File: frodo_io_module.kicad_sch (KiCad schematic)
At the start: 83 parts, among them J1 Molex MicroFit 2x3, J1 SWD, J2 Molex MicroFit 2x3, J4 JST-GH 4Pin, SW1 SW_DIP_x06, U1 AZ1117H-ADJ, U1 STM32F072RBT6, U3 AZ1117-3.3, U4 W25Q128JVP, U5 MCP2562-E-SN, U6 L7805, U7 L7805, Y1 8MHz 12pF

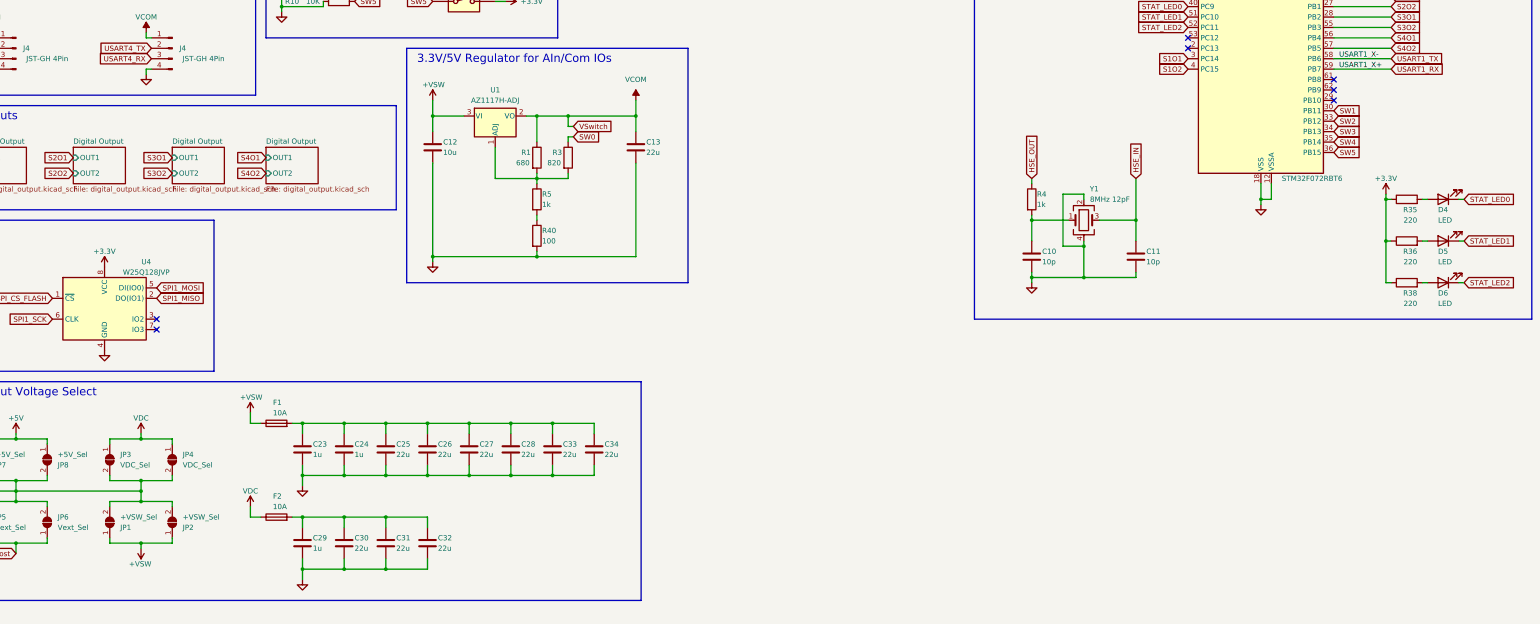
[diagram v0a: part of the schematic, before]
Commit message: Add boost converter schematics
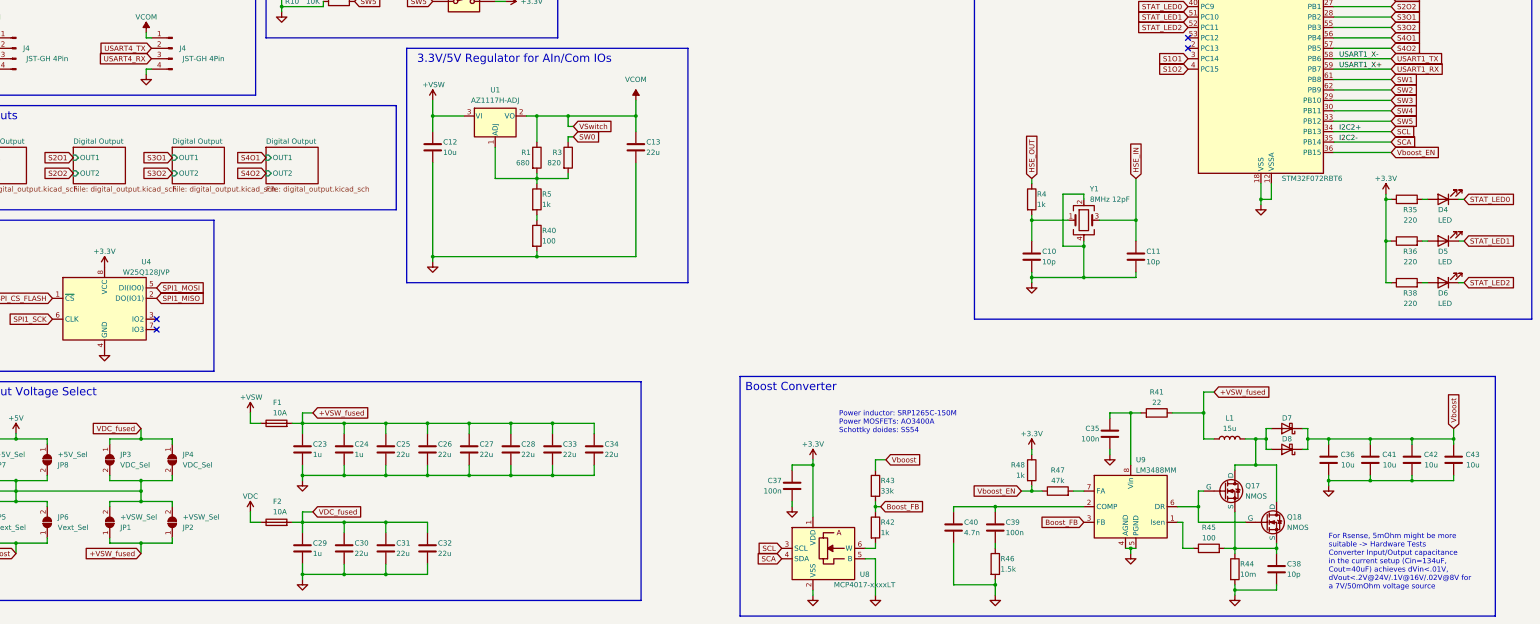
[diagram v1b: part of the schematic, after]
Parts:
- added C35, C37, C39: 100n, symbol Device:C
- added C36, C41, C42, C43: 10u, symbol Device:C
- added C38: 10p, symbol Device:C
- added C40: 4.7n, symbol Device:C
- added D7, D8: D_Schottky, symbol Device:D_Schottky
- added L1: 15u, symbol Device:L
- added Q17, Q18: NMOS, symbol Simulation_SPICE:NMOS
- added R41: 22, symbol Device:R
- added R42, R48: 1k, symbol Device:R
- added R43: 33k, symbol Device:R
- added R44: 10m, symbol Device:R
- added R45: 100, symbol Device:R
- added R46: 1.5k, symbol Device:R
- added R47: 47k, symbol Device:R
- added U8: MCP4017-xxxxLT, Package_TO_SOT_SMD:SOT-363_SC-70-6, symbol Potentiometer_Digital:MCP4017-xxxxLT
- added U9: LM3488MM, symbol frodo_io_module:LM3488MM
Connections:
- net +3.3V: now also C37.1, R48.1, U8.1 (VDD)
- net +VSW: no longer JP1.1 (A), JP2.1 (A)
- net GND: now also C35.2, C36.2, C37.2, C38.2, C40.2, C41.2, C42.2, C43.2, R44.2, R46.2, U8.2 (VSS), U8.5 (B), U9.4 (AGND), U9.5 (PGND)
- net SW1: now also U1.61 (PB8); no longer U1.30 (PB11)
- net SW2: now also U1.62 (PB9); no longer U1.33 (PB12)
- net SW3: now also U1.29 (PB10); no longer U1.34 (PB13)
- net SW4: now also U1.30 (PB11); no longer U1.35 (PB14)
- net SW5: now also U1.33 (PB12); no longer U1.36 (PB15)
- net VDC: no longer JP3.1 (A), JP4.1 (A)
- net Vboost: now also C36.1, C41.1, C42.1, C43.1, D7.1 (K), D8.1 (K), R43.1
- net +VSW_fused: now reaches C23.1, C24.1, C25.1, C26.1, C27.1, C28.1, C33.1, C34.1, F1.2
- net +VSW_fused: now also JP1.1 (A), JP2.1 (A), L1.1, R41.1
- net VDC_fused: now reaches C29.1, C30.1, C31.1, C32.1, F2.2
- net VDC_fused: now also JP3.1 (A), JP4.1 (A)
- new net: C35.1, R41.2, U9.8 (Vin)
- new net: R45.1, U9.1 (Isen)
- new net: C39.1, C40.1, U9.2 (COMP)
- new net: Q17.2 (G), Q18.2 (G), U9.6 (DR)
- new net: R47.2, U9.7 (FA)
- new net: D7.2 (A), D8.2 (A), L1.2, Q17.1 (D), Q18.1 (D)
- new net: C38.1, Q17.3 (S), Q18.3 (S), R44.1, R45.2
- new net: C39.2, R46.1
- new net: R42.2, U8.6 (W)
- new net Boost_FB: R42.1, R43.2, U9.3 (FB)
- new net SCA: U1.35 (PB14), U8.4 (SDA)
- new net SCL: U1.34 (PB13), U8.3 (SCL)
- new net Vboost_EN: R47.1, R48.2, U1.36 (PB15)
- no-connect marks 19 -> 16
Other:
- note added: "Boost Converter"
- note added: "For Rsense, 5mOhm might be more suitable -> Hardware Tests Converter Input/Output capacitance in the current setup (Cin=134uF, Cout=40uF) achieves dVin<.01V, dVout<.2V@24V/.1V@16V/.02V@8V for a 7V/50mOhm voltage source"
- note added: "Power inductor: SRP1265C-150M Power MOSFETs: AO3400A Schottky doides: SS54"
- moved on the sheet: C29, C30, C31, C32, F2

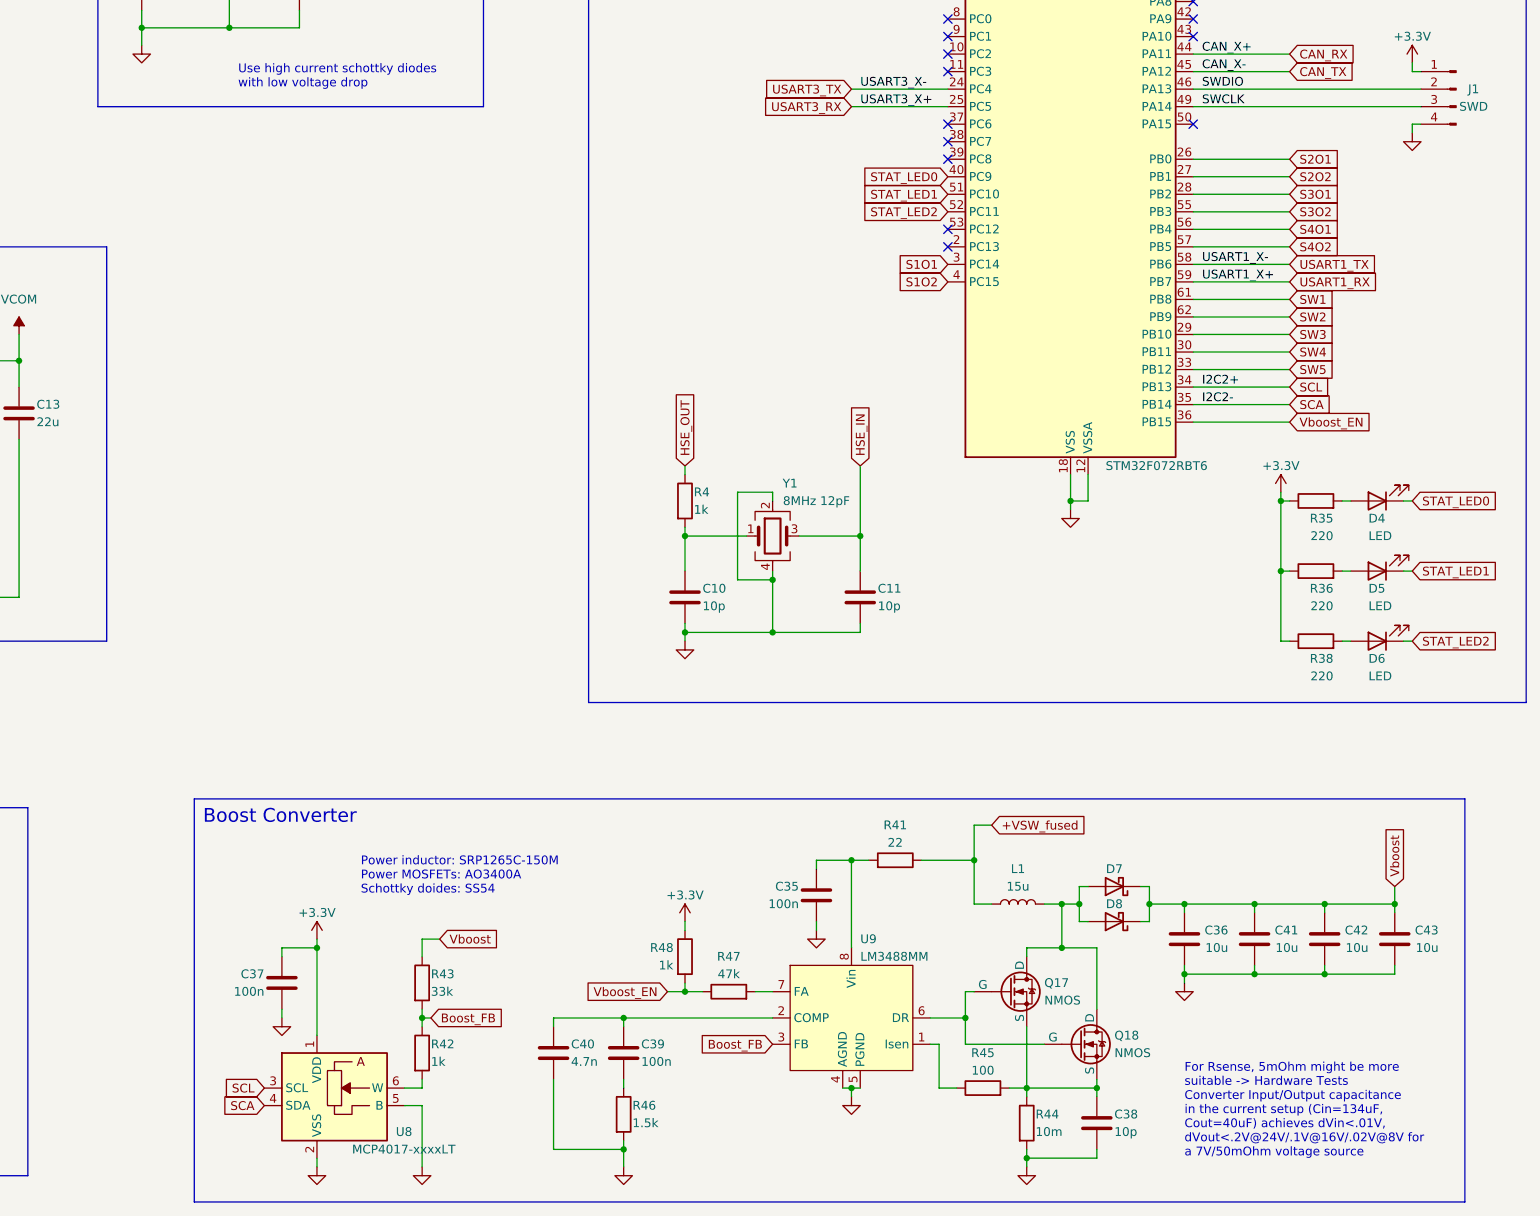
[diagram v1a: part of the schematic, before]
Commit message: Add test points
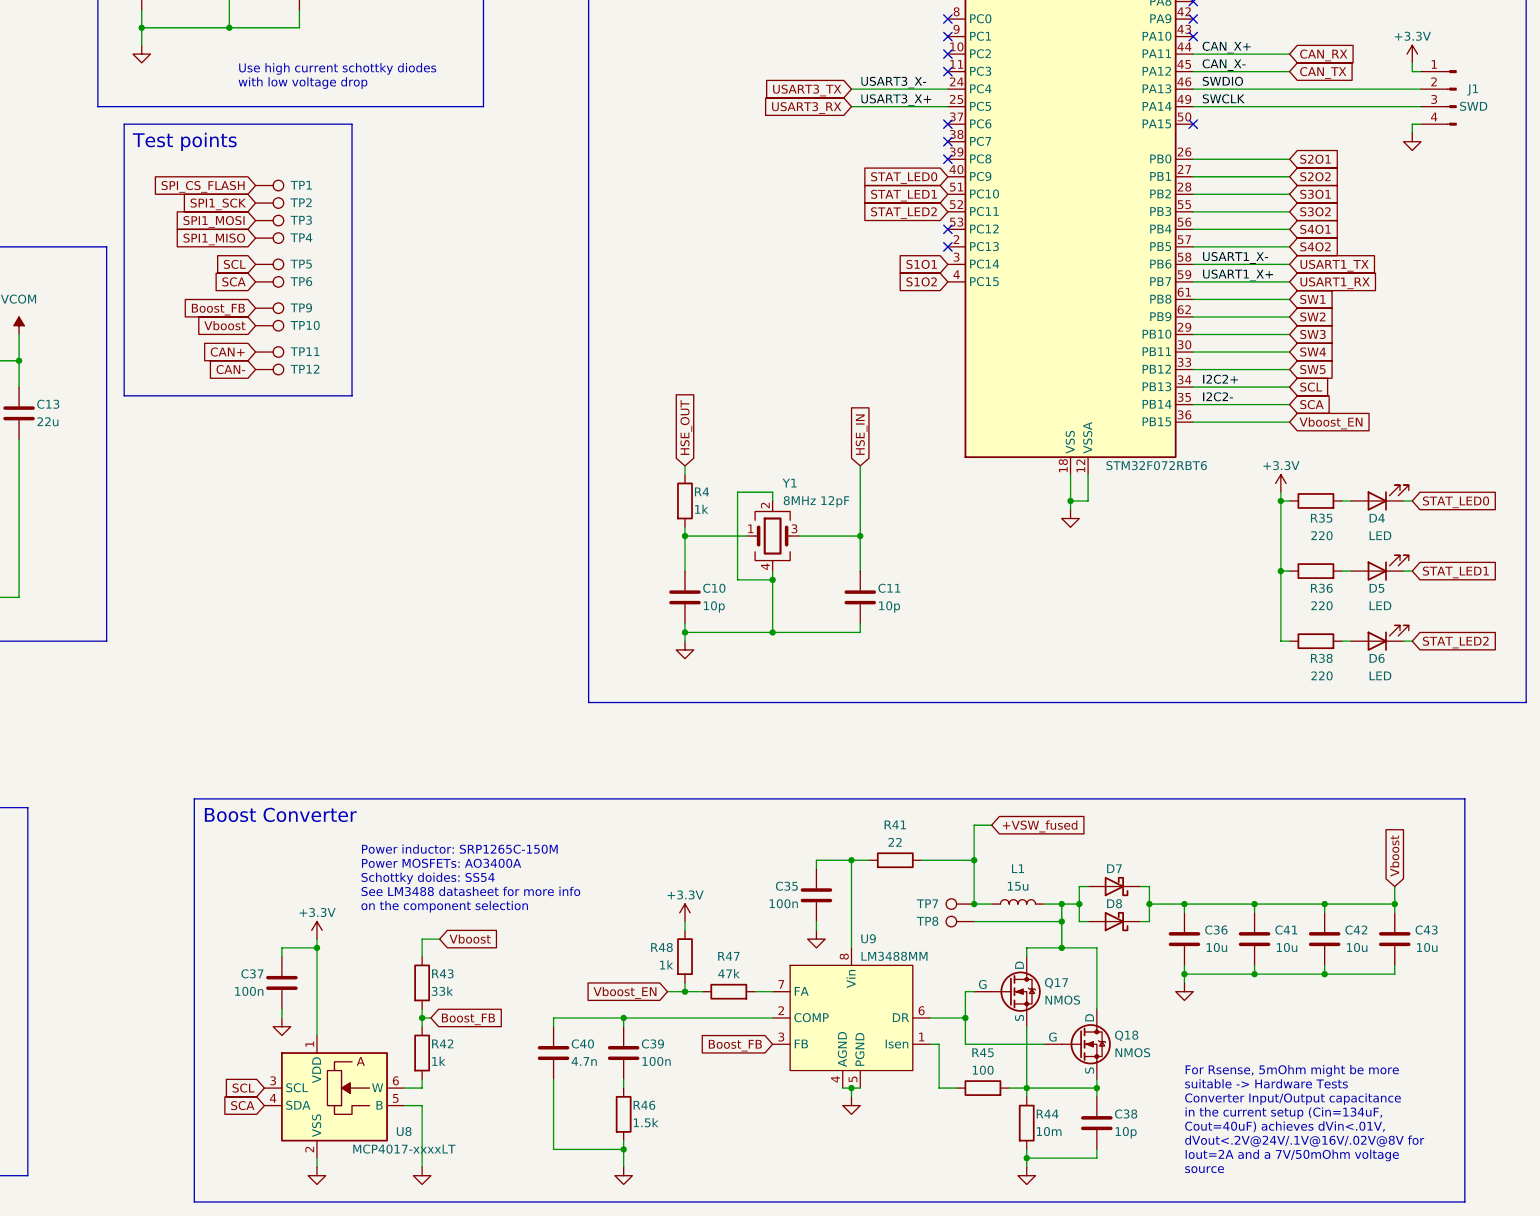
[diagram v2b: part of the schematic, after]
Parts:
- added TP1, TP10, TP11, TP12, TP2, TP3, TP4, TP5, TP6, TP7, TP8, TP9: TestPoint, symbol Connector:TestPoint
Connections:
- net +VSW_fused: now also TP7.1
- net Boost_FB: now also TP9.1
- net CAN+: now also TP11.1
- net CAN-: now also TP12.1
- net SCA: now also TP6.1
- net SCL: now also TP5.1
- net SPI1_MISO: now also TP4.1
- net SPI1_MOSI: now also TP3.1
- net SPI1_SCK: now also TP2.1
- net SPI_CS_FLASH: now also TP1.1
- net Vboost: now also TP10.1
- net at D7.2 (A), D8.2 (A), L1.2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: now also TP8.1
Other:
- note added: "For Rsense, 5mOhm might be more suitable -> Hardware Tests Converter Input/Output capacitance in the current setup (Cin=134uF, Cout=40uF) achieves dVin<.01V, dVout<.2V@24V/.1V@16V/.02V@8V for Iout=2A and a 7V/50mOhm voltage source"
- note added: "Power inductor: SRP1265C-150M Power MOSFETs: AO3400A Schottky doides: SS54 See LM3488 datasheet for more info on the component selection"
- note added: "Test points"
- note removed: "For Rsense, 5mOhm might be more suitable -> Hardware Tests Converter Input/Output capacitance in the current setup (Cin=134uF, Cout=40uF) achieves dVin<.01V, dVout<.2V@24V/.1V@16V/.02V@8V for a 7V/50mOhm voltage source"
- note removed: "Power inductor: SRP1265C-150M Power MOSFETs: AO3400A Schottky doides: SS54"

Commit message: Add I2C pull-up resistors and digital output flyback diodes
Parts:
- added R49, R50, R51, R52: 4.7k, symbol Device:R
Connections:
- net +3.3V: now also R49.1, R50.1, R51.1, R52.1
- net SCA: now also R52.2
- net SCL: now also R51.2
- net USART1_RX: now also R50.2
- net USART1_TX: now also R49.2
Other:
- note added: "Pull-Ups for the use of I2C"
- moved on the sheet: R10, R6, R7, R8, R9, SW1
